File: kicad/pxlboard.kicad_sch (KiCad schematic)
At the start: 68 parts, among them U1 XIAO-RP2040-SMD, U2 LIS3DHTR

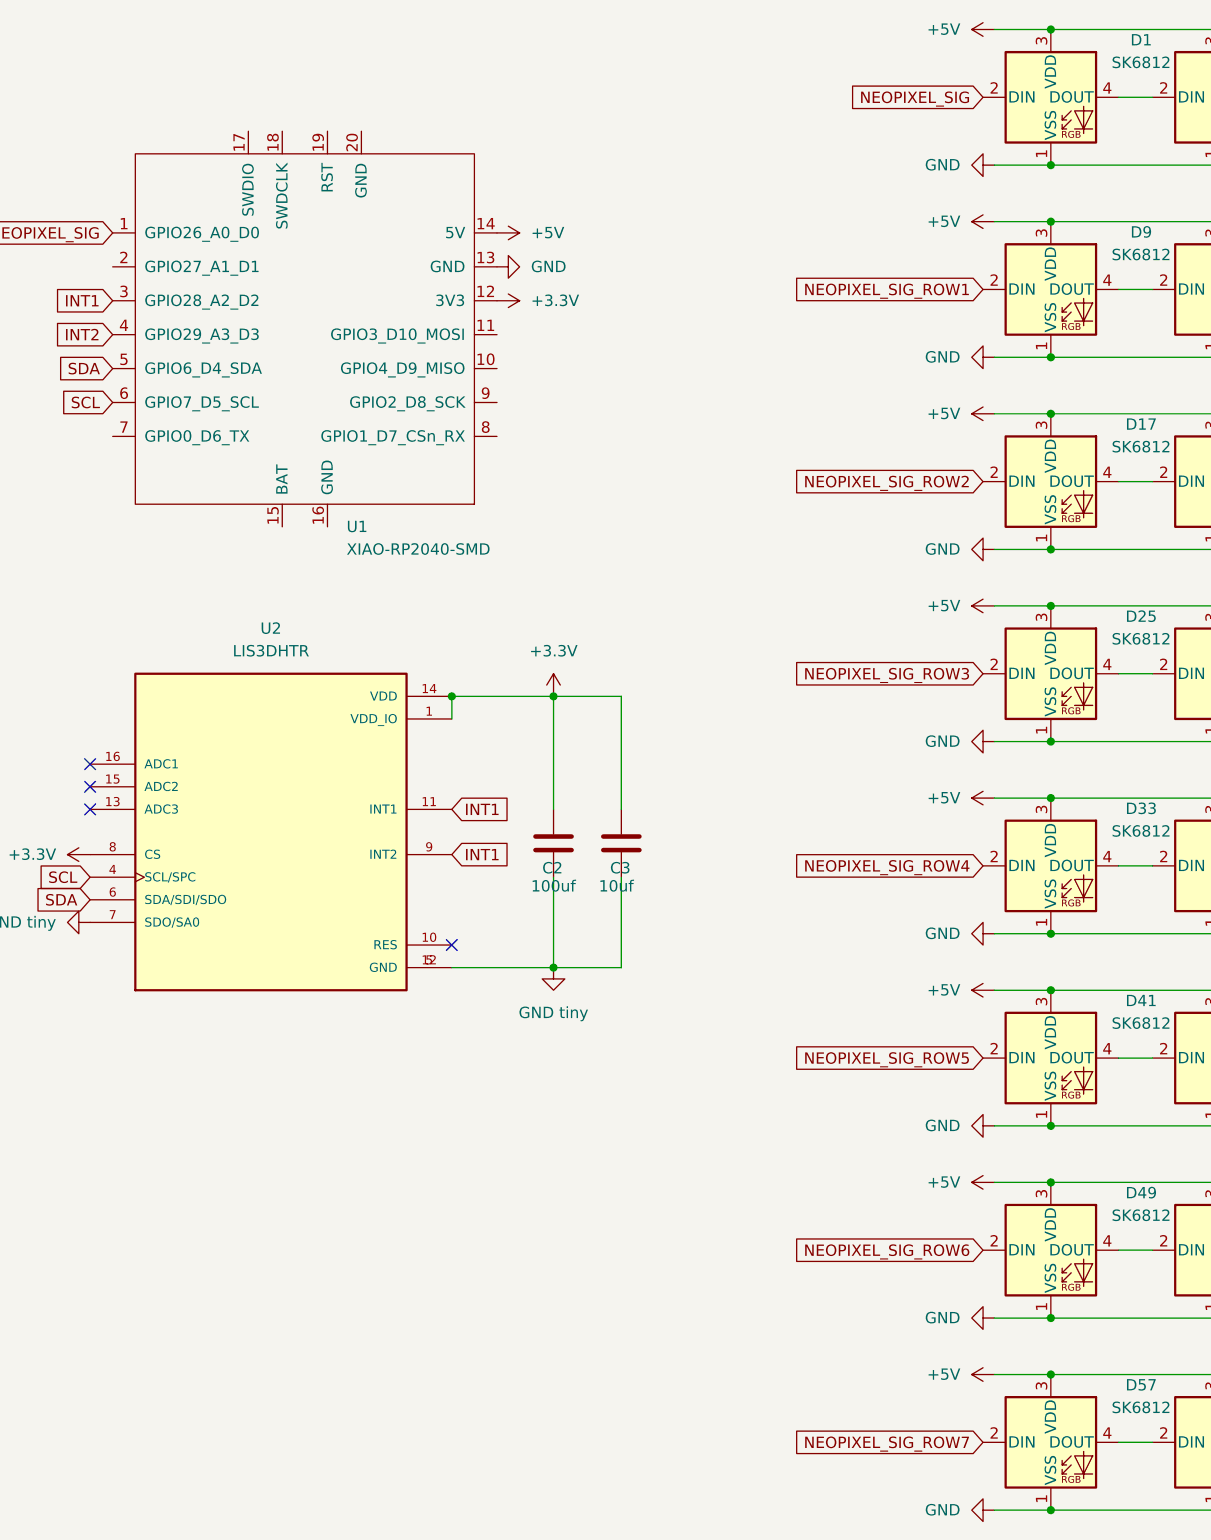
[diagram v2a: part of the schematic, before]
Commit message: feat: add caps and reroute
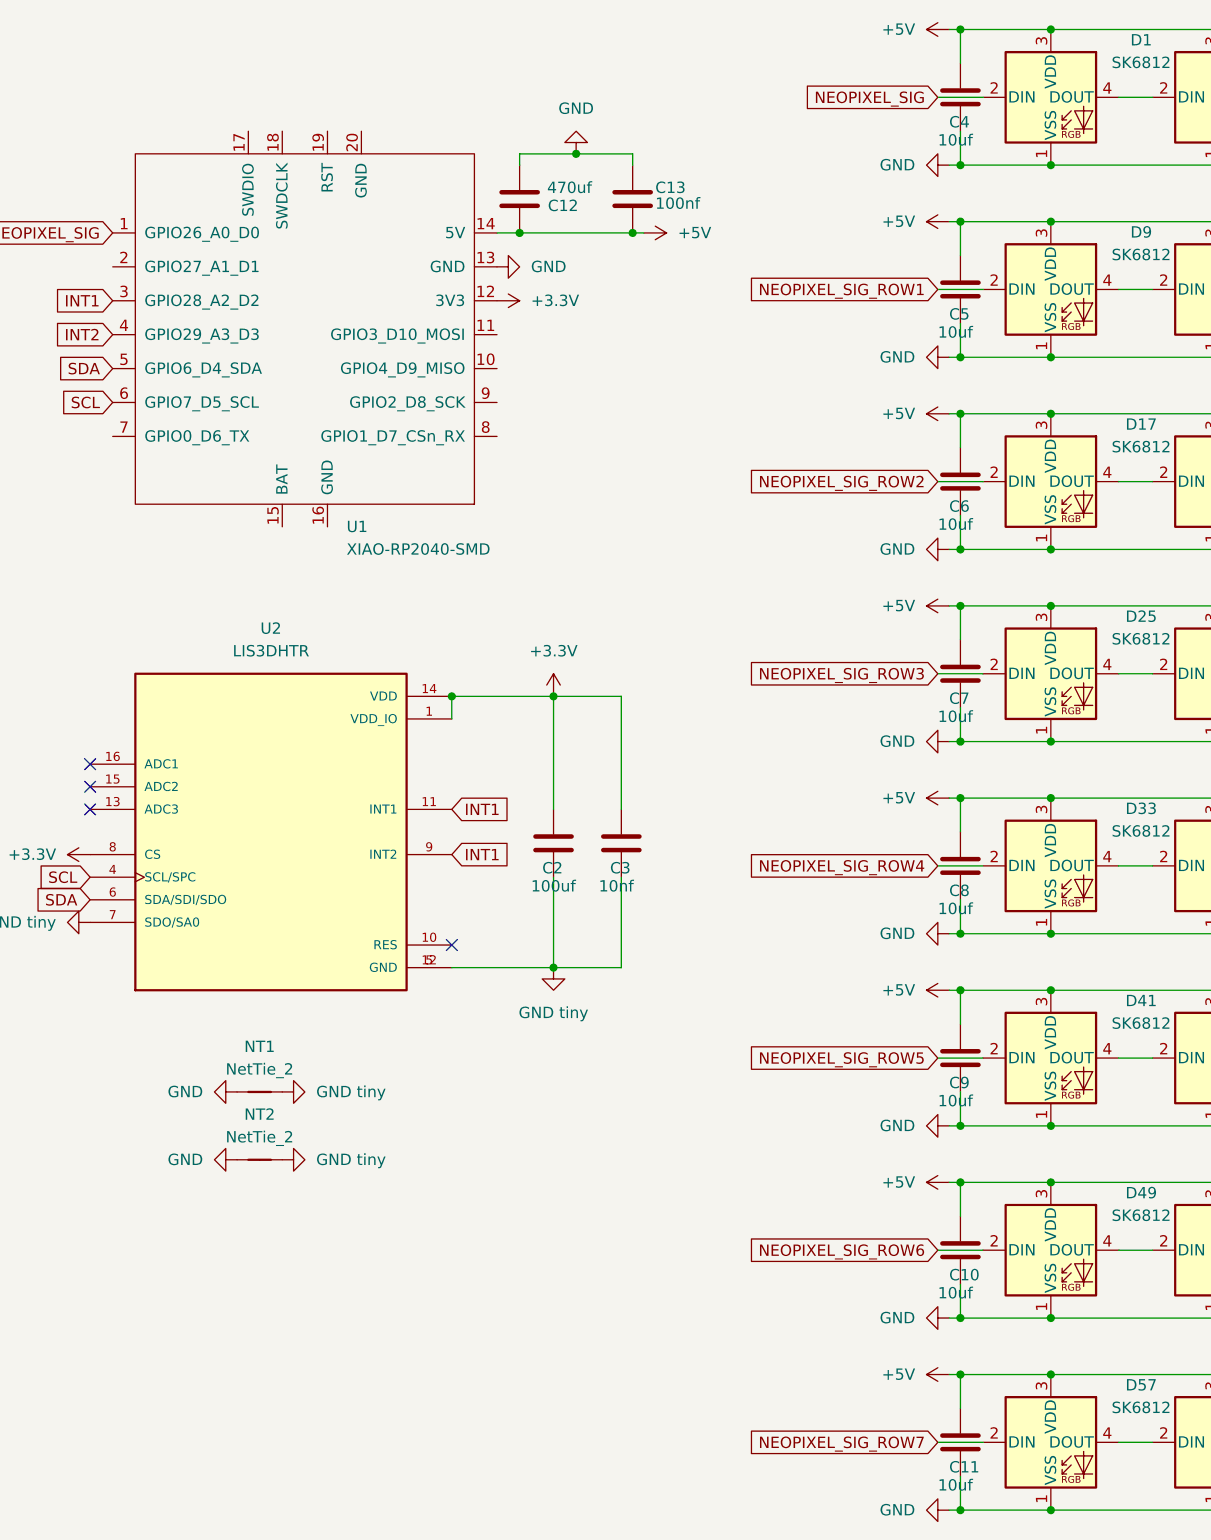
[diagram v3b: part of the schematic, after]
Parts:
- added C10, C11, C4, C5, C6, C7, C8, C9: 10uf, Capacitor_SMD:C_1206_3216Metric_Pad1.33x1.80mm_HandSolder, symbol Device:C
- added C12: 470uf, Capacitor_SMD:CP_Elec_6.3x9.9, symbol Device:C
- added C13: 100nf, Capacitor_SMD:C_1206_3216Metric_Pad1.33x1.80mm_HandSolder, symbol Device:C
- added NT1, NT2: NetTie_2, NetTie:NetTie-2_SMD_Pad0.5mm, symbol Device:NetTie_2
- C3: value 10uf -> 10nf; footprint Capacitor_SMD:C_0402_1005Metric_Pad0.74x0.62mm_HandSolder -> Capacitor_SMD:C_1206_3216Metric_Pad1.33x1.80mm_HandSolder
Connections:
- net +5V: now also C10.1, C11.1, C12.1, C13.2, C4.1, C5.1, C6.1, C7.1, C8.1, C9.1
- net GND: now also C10.2, C11.2, C12.2, C13.1, C4.2, C5.2, C6.2, C7.2, C8.2, C9.2, NT1.1, NT2.1
- net GND tiny: now also NT1.2, NT2.2

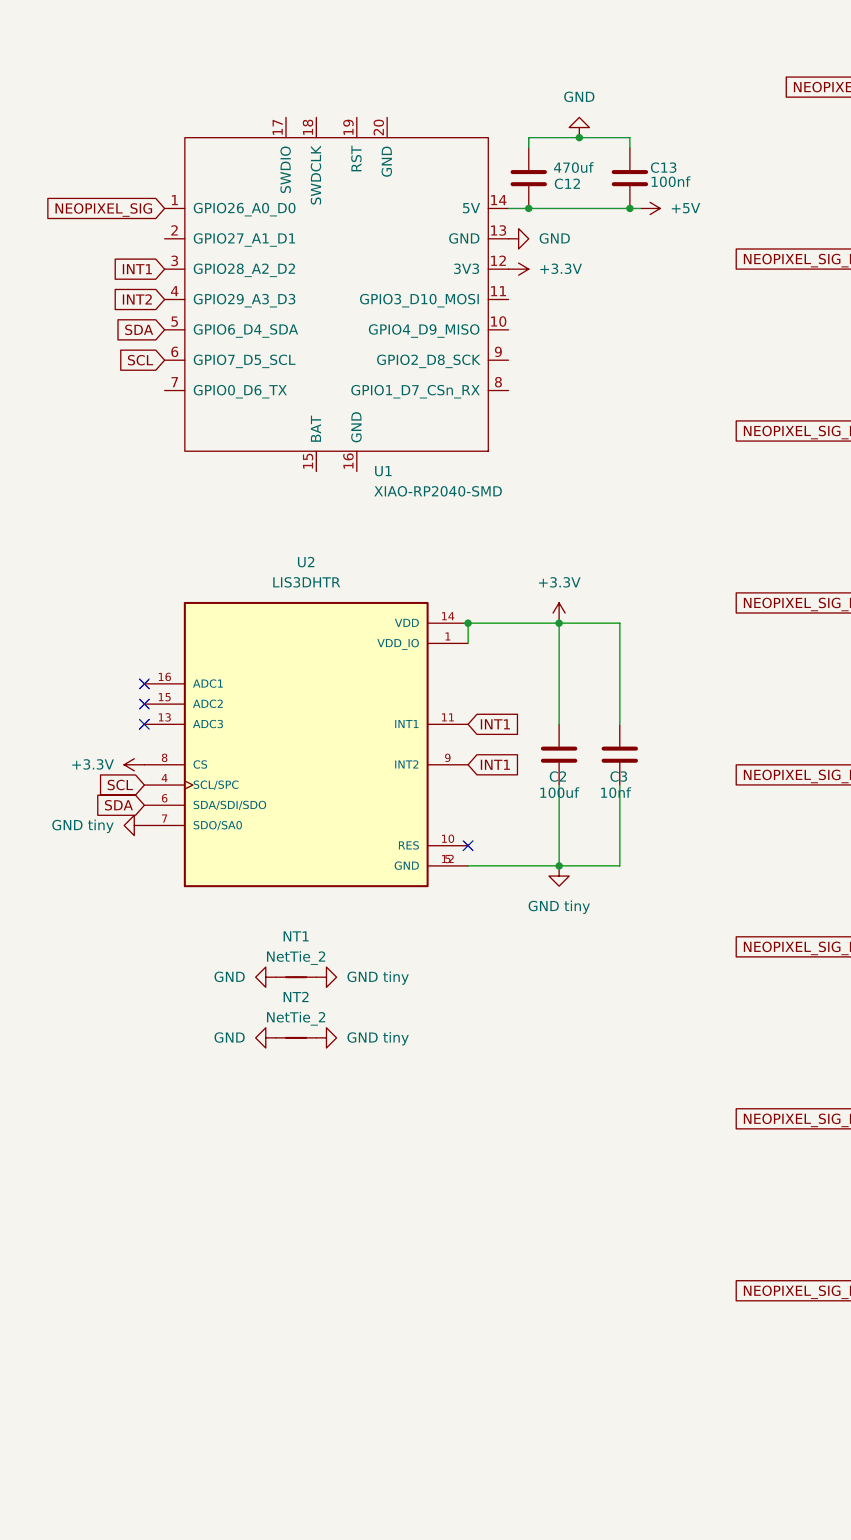
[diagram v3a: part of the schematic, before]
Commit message: feat: add power usb c
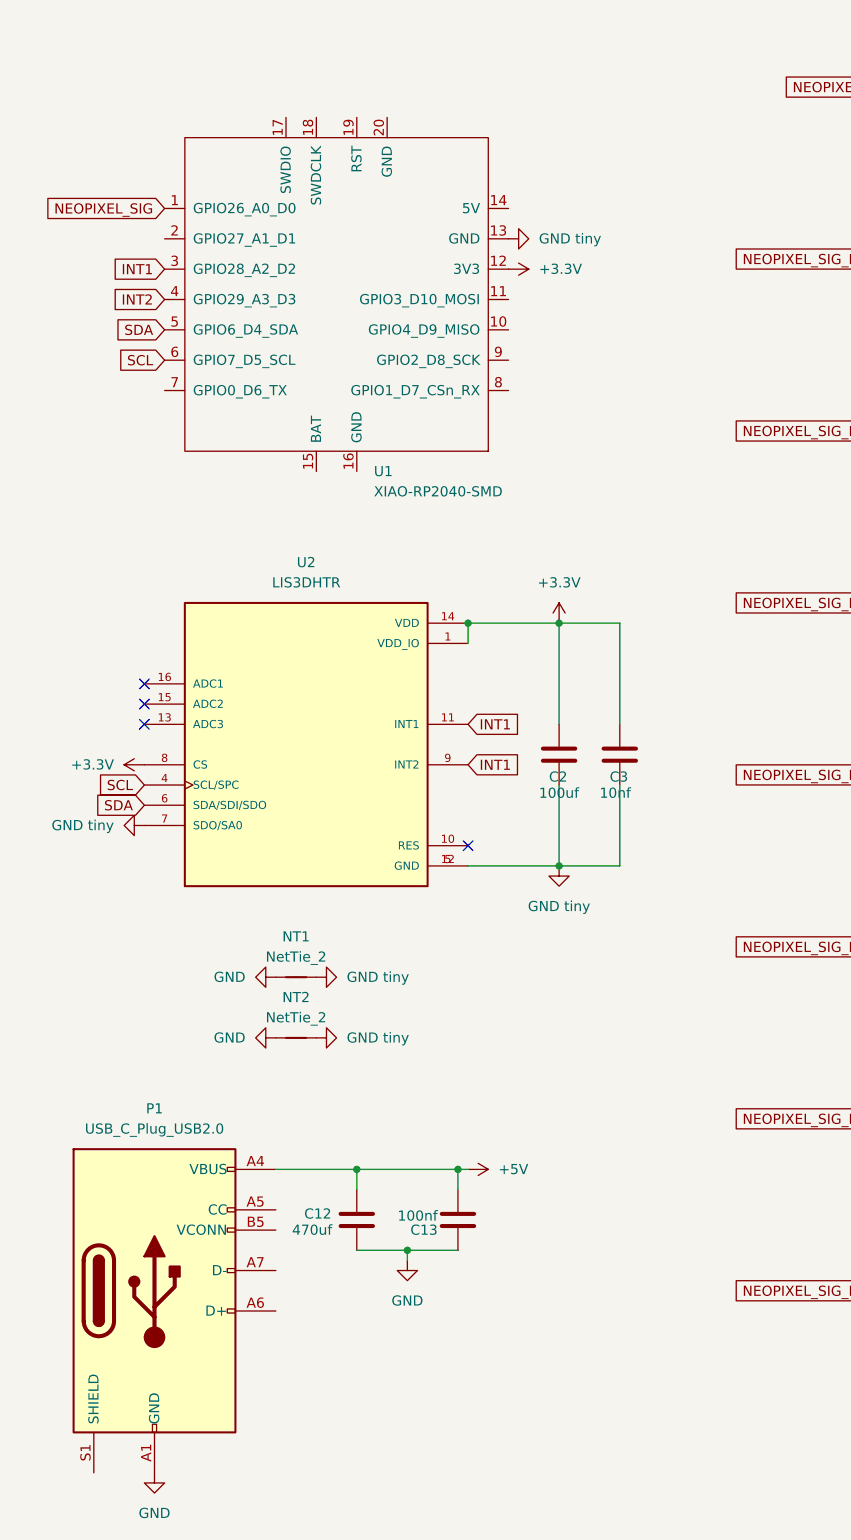
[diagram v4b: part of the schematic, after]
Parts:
- added P1: USB_C_Plug_USB2.0, lib:TYPE-C-31-M-12, symbol Connector:USB_C_Plug_USB2.0
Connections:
- net +5V: now also P1.A4 (VBUS), P1.A9 (VBUS), P1.B4 (VBUS), P1.B9 (VBUS); no longer U1.14 (5V)
- net GND: now also P1.A1 (GND), P1.A12 (GND), P1.B1 (GND), P1.B12 (GND); no longer U1.13 (GND)
- net GND tiny: now also U1.13 (GND)
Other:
- moved on the sheet: C12, C13
